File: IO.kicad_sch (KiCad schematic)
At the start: 7 parts

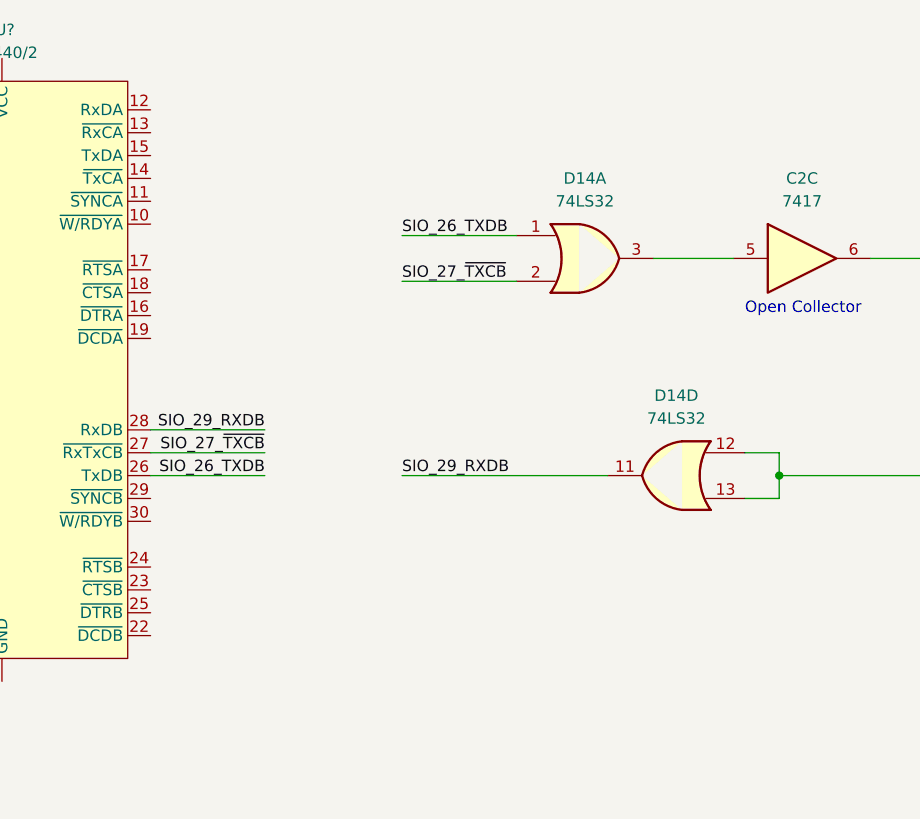
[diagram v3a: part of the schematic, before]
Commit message: Add SIOCLK jumper detail jumper details.
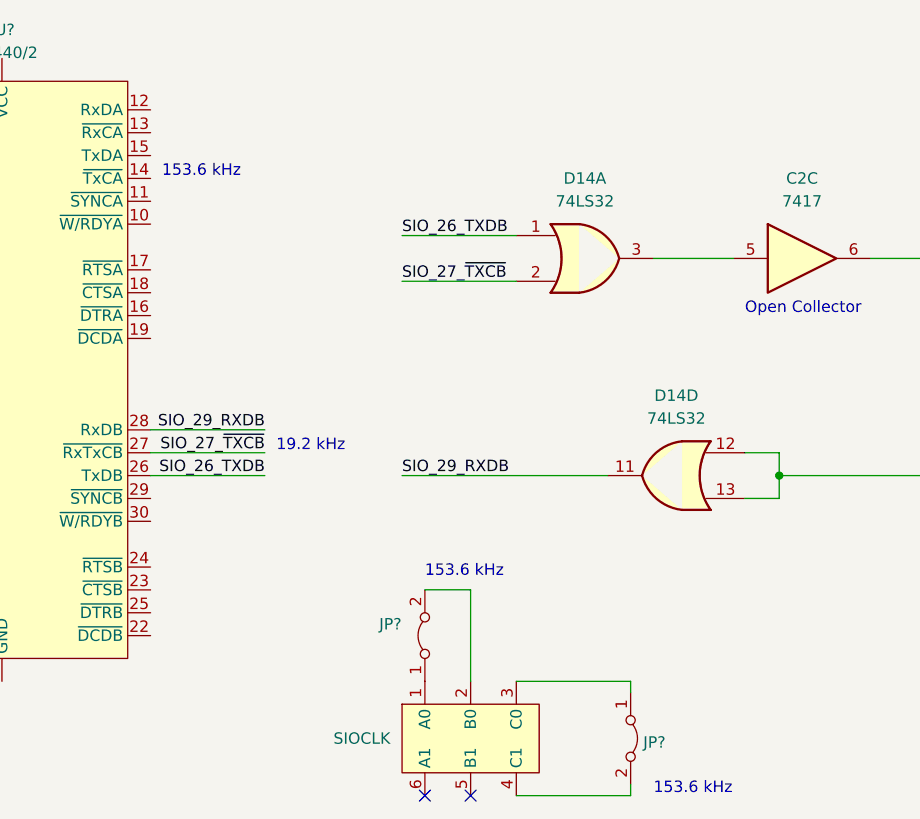
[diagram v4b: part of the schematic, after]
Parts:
- added J?: SIOCLK, symbol ceda:SIOCLK
- added JP? (x2): Jumper_2_Bridged, symbol Jumper:Jumper_2_Bridged
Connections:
- new net: J?.1 (A0), JP?.1 (A)
- new net: J?.2 (B0), JP?.2 (B)
- new net: J?.3 (C0), JP?.1 (A)
- new net: J?.4 (C1), JP?.2 (B)
- no-connect marks 0 -> 2
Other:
- note added: "153.6 kHz"
- note added: "19.2 kHz"
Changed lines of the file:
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@@
   (junction (at 167.64 54.61) (diameter 0) (color 0 0 0 0)
   )
+  (no_connect (at 78.74 114.3))
+  (no_connect (at 83.82 114.3))
   (wire (pts (xy 143.51 77.47) (xy 143.51 78.74))
     (stroke (width 0) (type default) (color 0 0 0 0))
@@
     (stroke (width 0) (type default) (color 0 0 0 0))
   )
+  (wire (pts (xy 88.9 114.3) (xy 101.6 114.3))
+    (stroke (width 0) (type default) (color 0 0 0 0))
+  )
   (wire (pts (xy 48.26 78.74) (xy 60.96 78.74))
     (stroke (width 0) (type default) (color 0 0 0 0))
@@
     (stroke (width 0) (type default) (color 0 0 0 0))
   )
+  (wire (pts (xy 101.6 114.3) (xy 101.6 113.03))
+    (stroke (width 0) (type default) (color 0 0 0 0))
+  )
   (wire (pts (xy 118.11 78.74) (xy 118.11 76.2))
     (stroke (width 0) (type default) (color 0 0 0 0))
@@
     (stroke (width 0) (type default) (color 0 0 0 0))
   )
+  (wire (pts (xy 101.6 101.6) (xy 101.6 102.87))
+    (stroke (width 0) (type default) (color 0 0 0 0))
+  )
   (wire (pts (xy 143.51 44.45) (xy 143.51 45.72))
     (stroke (width 0) (type default) (color 0 0 0 0))
@@
     (stroke (width 0) (type default) (color 0 0 0 0))
   )
+  (wire (pts (xy 78.74 91.44) (xy 83.82 91.44))
+    (stroke (width 0) (type default) (color 0 0 0 0))
+  )
   (wire (pts (xy 104.14 54.61) (xy 113.03 54.61))
     (stroke (width 0) (type default) (color 0 0 0 0))
   )
+  (wire (pts (xy 83.82 91.44) (xy 83.82 101.6))
+    (stroke (width 0) (type default) (color 0 0 0 0))
+  )
   (wire (pts (xy 167.64 62.23) (xy 167.64 54.61))
     (stroke (width 0) (type default) (color 0 0 0 0))
@@
     (stroke (width 0) (type default) (color 0 0 0 0))
   )
+  (wire (pts (xy 88.9 101.6) (xy 101.6 101.6))
+    (stroke (width 0) (type default) (color 0 0 0 0))
+  )
   (wire (pts (xy 76.2 52.07) (xy 88.9 52.07))
     (stroke (width 0) (type default) (color 0 0 0 0))
@@
   (wire (pts (xy 229.87 69.85) (xy 238.76 69.85))
     (stroke (width 0) (type default) (color 0 0 0 0))
+  )
+  (text "153.6 kHz" (at 104.14 114.3 0)
+    (effects (font (size 1.27 1.27)) (justify left bottom))
   )
   (text "Open Collector" (at 114.3 60.96 0)
@@
   (text "In realtà non ho idea di\nquale siano rx e tx, visto\nche sono cortocircuitati"
     (at 278.13 72.39 0)
+    (effects (font (size 1.27 1.27)) (justify left bottom))
+  )
+  (text "153.6 kHz" (at 49.53 45.72 0)
+    (effects (font (size 1.27 1.27)) (justify left bottom))
+  )
+  (text "153.6 kHz" (at 78.74 90.17 0)
+    (effects (font (size 1.27 1.27)) (justify left bottom))
+  )
+  (text "19.2 kHz" (at 62.23 76.2 0)
     (effects (font (size 1.27 1.27)) (justify left bottom))
   )
@@
     (pin "14")
     (pin "7")
+  )
+  (symbol (lib_id "ceda:SIOCLK") (at 83.82 107.95 0) (unit 1)
+    (in_bom yes) (on_board yes)
+    (property "Reference" "J?" (id 0) (at 72.39 105.41 0)
+      (effects (font (size 1.27 1.27)) (justify left) hide)
+    )
+    (property "Value" "SIOCLK" (id 1) (at 68.58 107.95 0)
+      (effects (font (size 1.27 1.27)) (justify left))
+    )
+    (property "Footprint" "" (id 2) (at 83.82 107.95 0)
+      (effects (font (size 1.27 1.27)) hide)
+    )
+    (property "Datasheet" "" (id 3) (at 83.82 107.95 0)
+      (effects (font (size 1.27 1.27)) hide)
+    )
+    (pin "1")
+    (pin "2")
+    (pin "3")
+    (pin "4")
+    (pin "5")
+    (pin "6")
   )
   (symbol (lib_id "power:+5V") (at 143.51 44.45 0) (unit 1)
@@
     (pin "8")
     (pin "9")
+  )
+  (symbol (lib_id "Jumper:Jumper_2_Bridged") (at 101.6 107.95 270) (unit 1)
+    (in_bom yes) (on_board yes) (fields_autoplaced)
+    (property "Reference" "JP?" (id 0) (at 102.997 108.3838 90)
+      (effects (font (size 1.27 1.27)) (justify left))
+    )
+    (property "Value" "Jumper_2_Bridged" (id 1) (at 102.997 109.6522 90)
+      (effects (font (size 1.27 1.27)) (justify left) hide)
+    )
+    (property "Footprint" "" (id 2) (at 101.6 107.95 0)
+      (effects (font (size 1.27 1.27)) hide)
+    )
+    (property "Datasheet" "~" (id 3) (at 101.6 107.95 0)
+      (effects (font (size 1.27 1.27)) hide)
+    )
+    (pin "1")
+    (pin "2")
   )
   (symbol (lib_id "power:+5V") (at 143.51 68.58 0) (unit 1)
@@
       (effects (font (size 1.27 1.27)) hide)
     )
+    (pin "1")
+    (pin "2")
+  )
+  (symbol (lib_id "Jumper:Jumper_2_Bridged") (at 78.74 96.52 90) (unit 1)
+    (in_bom yes) (on_board yes)
+    (property "Reference" "JP?" (id 0) (at 73.66 95.25 90)
+      (effects (font (size 1.27 1.27)) (justify right))
+    )
+    (property "Value" "Jumper_2_Bridged" (id 1) (at 59.69 97.79 90)
+      (effects (font (size 1.27 1.27)) (justify right) hide)
+    )
+    (property "Footprint" "" (id 2) (at 78.74 96.52 0)
+      (effects (font (size 1.27 1.27)) hide)
+    )
+    (property "Datasheet" "~" (id 3) (at 78.74 96.52 0)
+      (effects (font (size 1.27 1.27)) hide)
+    )

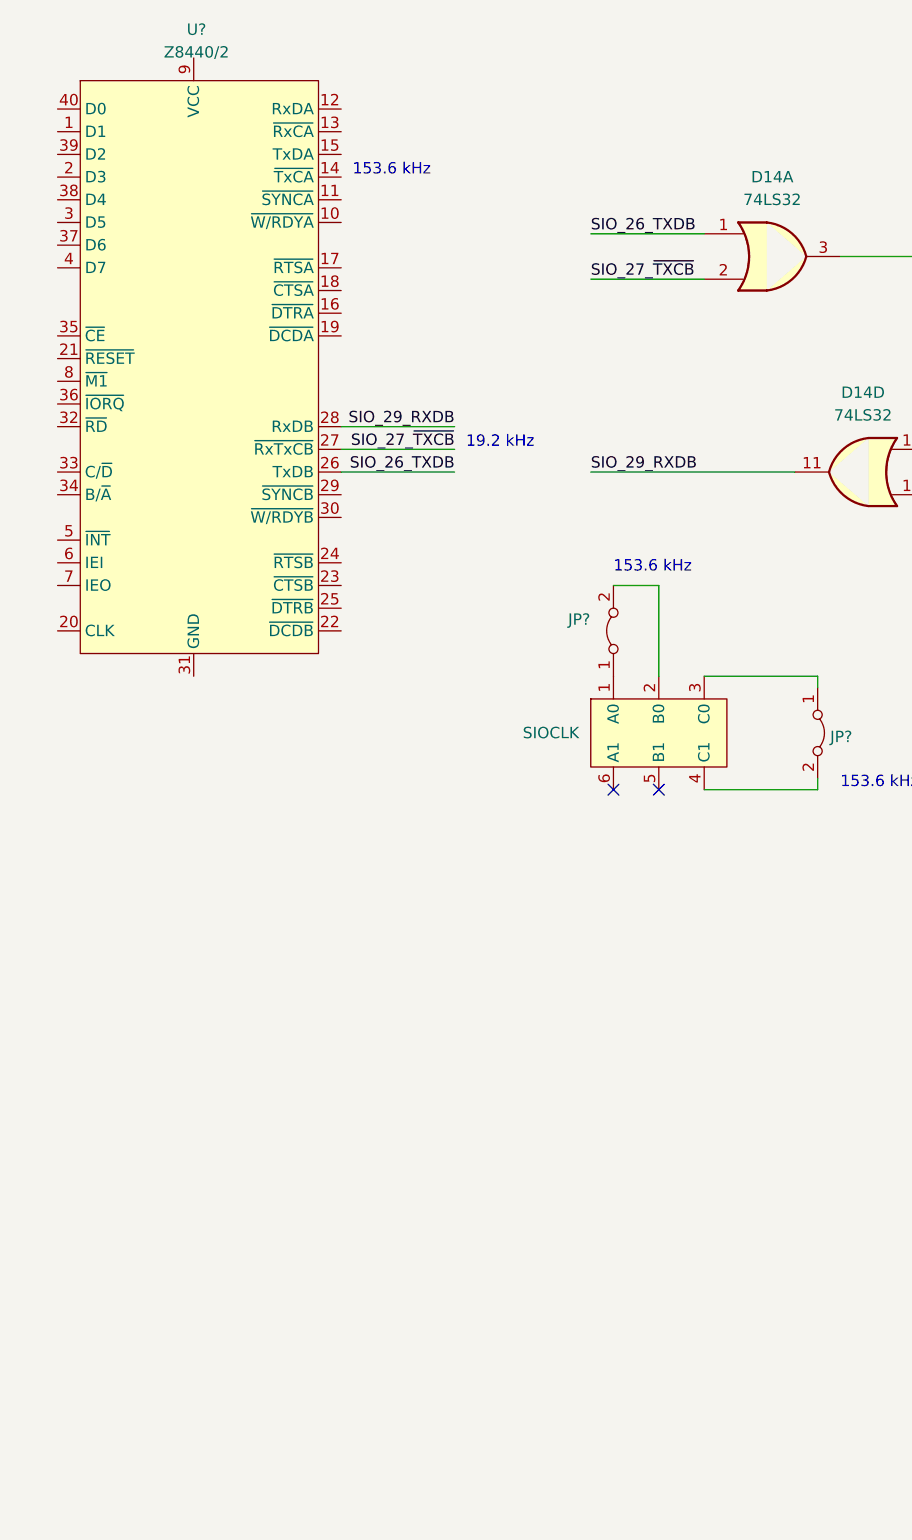
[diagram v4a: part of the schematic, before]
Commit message: Add address wires for SIO.
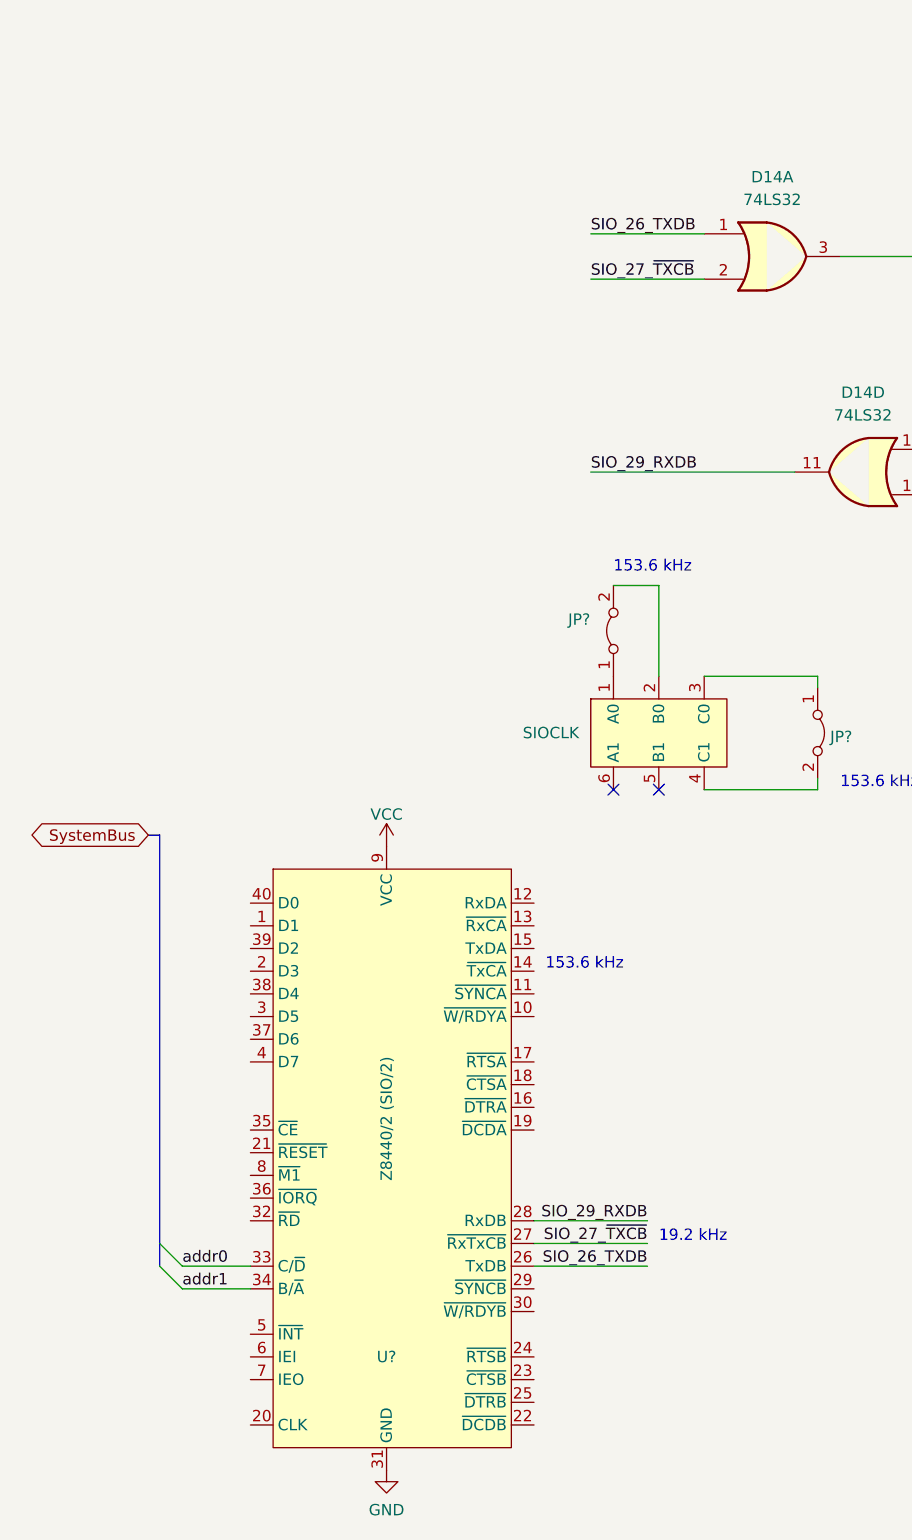
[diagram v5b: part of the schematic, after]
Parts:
- U?: value Z8440/2 -> Z8440/2 (SIO/2)
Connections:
- net GND: now reaches U?.31 (GND)
- net addr0: now reaches U?.33 (C/~{D})
- net addr1: now reaches U?.34 (B/~{A})
- net VCC: now reaches U?.9 (VCC)
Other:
- moved on the sheet: U?
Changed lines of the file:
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@@
   (no_connect (at 78.74 114.3))
   (no_connect (at 83.82 114.3))
+  (bus_entry (at 27.94 165.1) (size 2.54 2.54)
+    (stroke (width 0) (type default) (color 0 0 0 0))
+  )
+  (bus_entry (at 27.94 167.64) (size 2.54 2.54)
+    (stroke (width 0) (type default) (color 0 0 0 0))
+  )
   (wire (pts (xy 143.51 77.47) (xy 143.51 78.74))
     (stroke (width 0) (type default) (color 0 0 0 0))
@@
     (stroke (width 0) (type default) (color 0 0 0 0))
   )
-  (wire (pts (xy 48.26 78.74) (xy 60.96 78.74))
+  (wire (pts (xy 69.85 167.64) (xy 82.55 167.64))
     (stroke (width 0) (type default) (color 0 0 0 0))
   )
@@
     (stroke (width 0) (type default) (color 0 0 0 0))
   )
+  (wire (pts (xy 30.48 170.18) (xy 38.1 170.18))
+    (stroke (width 0) (type default) (color 0 0 0 0))
+  )
+  (wire (pts (xy 30.48 167.64) (xy 38.1 167.64))
+    (stroke (width 0) (type default) (color 0 0 0 0))
+  )
   (wire (pts (xy 232.41 41.91) (xy 238.76 41.91))
     (stroke (width 0) (type default) (color 0 0 0 0))
@@
     (stroke (width 0) (type default) (color 0 0 0 0))
   )
-  (wire (pts (xy 48.26 73.66) (xy 60.96 73.66))
+  (wire (pts (xy 69.85 162.56) (xy 82.55 162.56))
     (stroke (width 0) (type default) (color 0 0 0 0))
   )
@@
     (stroke (width 0) (type default) (color 0 0 0 0))
   )
+  (bus (pts (xy 26.67 119.38) (xy 27.94 119.38))
+    (stroke (width 0) (type default) (color 0 0 0 0))
+  )
   (wire (pts (xy 194.31 54.61) (xy 167.64 54.61))
     (stroke (width 0) (type default) (color 0 0 0 0))
@@
     (stroke (width 0) (type default) (color 0 0 0 0))
   )
+  (bus (pts (xy 27.94 167.64) (xy 27.94 165.1))
+    (stroke (width 0) (type default) (color 0 0 0 0))
+  )
   (wire (pts (xy 104.14 54.61) (xy 113.03 54.61))
     (stroke (width 0) (type default) (color 0 0 0 0))
@@
     (stroke (width 0) (type default) (color 0 0 0 0))
   )
+  (bus (pts (xy 27.94 165.1) (xy 27.94 119.38))
+    (stroke (width 0) (type default) (color 0 0 0 0))
+  )
   (wire (pts (xy 251.46 41.91) (xy 257.81 41.91))
     (stroke (width 0) (type default) (color 0 0 0 0))
@@
     (stroke (width 0) (type default) (color 0 0 0 0))
   )
-  (wire (pts (xy 48.26 76.2) (xy 60.96 76.2))
+  (wire (pts (xy 69.85 165.1) (xy 82.55 165.1))
     (stroke (width 0) (type default) (color 0 0 0 0))
   )
@@
     (effects (font (size 1.27 1.27)) (justify left bottom))
   )
-  (text "153.6 kHz" (at 49.53 45.72 0)
+  (text "153.6 kHz" (at 71.12 134.62 0)
     (effects (font (size 1.27 1.27)) (justify left bottom))
   )
@@
     (effects (font (size 1.27 1.27)) (justify left bottom))
   )
-  (text "19.2 kHz" (at 62.23 76.2 0)
+  (text "19.2 kHz" (at 83.82 165.1 0)
     (effects (font (size 1.27 1.27)) (justify left bottom))
   )
@@
     (effects (font (size 1.27 1.27)) (justify right bottom))
   )
-  (label "SIO_29_RXDB" (at 60.96 73.66 180)
-    (effects (font (size 1.27 1.27)) (justify right bottom))
+  (label "SIO_29_RXDB" (at 82.55 162.56 180)
+    (effects (font (size 1.27 1.27)) (justify right bottom))
+  )
+  (label "addr1" (at 30.48 170.18 0)
+    (effects (font (size 1.27 1.27)) (justify left bottom))
   )
   (label "SIO_26_TXDB" (at 76.2 52.07 0)
     (effects (font (size 1.27 1.27)) (justify left bottom))
   )
-  (label "SIO_26_TXDB" (at 60.96 78.74 180)
-    (effects (font (size 1.27 1.27)) (justify right bottom))
-  )
-  (label "SIO_27_~{TXCB}" (at 60.96 76.2 180)
+  (label "SIO_26_TXDB" (at 82.55 167.64 180)
+    (effects (font (size 1.27 1.27)) (justify right bottom))
+  )
+  (label "SIO_27_~{TXCB}" (at 82.55 165.1 180)
     (effects (font (size 1.27 1.27)) (justify right bottom))
   )
@@
     (effects (font (size 1.27 1.27)) (justify right bottom))
   )
+  (label "addr0" (at 30.48 167.64 0)
+    (effects (font (size 1.27 1.27)) (justify left bottom))
+  )
   (label "KBD_TX" (at 260.35 69.85 180)
     (effects (font (size 1.27 1.27)) (justify right bottom))
+  )
+  (global_label "SystemBus" (shape bidirectional) (at 26.67 119.38 180) (fields_autoplaced)
+    (effects (font (size 1.27 1.27)) (justify right))
+    (property "Riferimenti inter-foglio" "${INTERSHEET_REFS}" (id 0) (at 14.0969 119.3006 0)
+      (effects (font (size 1.27 1.27)) (justify right) hide)
+    )
   )
   (symbol (lib_id "74xx:74LS32") (at 106.68 78.74 0) (mirror y) (unit 4)
@@
     (pin "7")
   )
+  (symbol (lib_id "power:GND") (at 53.34 190.5 0) (unit 1)
+    (in_bom yes) (on_board yes) (fields_autoplaced)
+    (property "Reference" "#PWR?" (id 0) (at 53.34 196.85 0)
+      (effects (font (size 1.27 1.27)) hide)
+    )
+    (property "Value" "GND" (id 1) (at 53.34 194.9434 0))
+    (property "Footprint" "" (id 2) (at 53.34 190.5 0)
+      (effects (font (size 1.27 1.27)) hide)
+    )
+    (property "Datasheet" "" (id 3) (at 53.34 190.5 0)
+      (effects (font (size 1.27 1.27)) hide)
+    )
+    (pin "1")
+  )
   (symbol (lib_id "ceda:SIOCLK") (at 83.82 107.95 0) (unit 1)
     (in_bom yes) (on_board yes)
@@
     (pin "1")
   )
-  (symbol (lib_id "ceda:Z8440{slash}2") (at 31.75 63.5 0) (unit 1)
-    (in_bom yes) (on_board yes) (fields_autoplaced)
-    (property "Reference" "U?" (id 0) (at 32.0675 29.21 0))
-    (property "Value" "Z8440/2" (id 1) (at 32.0675 31.75 0))
-    (property "Footprint" "" (id 2) (at 26.035 48.895 0)
-      (effects (font (size 1.27 1.27)) hide)
-    )
-    (property "Datasheet" "" (id 3) (at 26.035 48.895 0)
-      (effects (font (size 1.27 1.27)) hide)
-    )
+  (symbol (lib_id "power:VCC") (at 53.34 120.65 0) (unit 1)
+    (in_bom yes) (on_board yes) (fields_autoplaced)
+    (property "Reference" "#PWR?" (id 0) (at 53.34 124.46 0)
+      (effects (font (size 1.27 1.27)) hide)
+    )
+    (property "Value" "VCC" (id 1) (at 53.34 117.0742 0))
+    (property "Footprint" "" (id 2) (at 53.34 120.65 0)
+      (effects (font (size 1.27 1.27)) hide)
+    )
+    (property "Datasheet" "" (id 3) (at 53.34 120.65 0)
+      (effects (font (size 1.27 1.27)) hide)
+    )
+    (pin "1")
+  )
+  (symbol (lib_id "ceda:Z8440{slash}2") (at 53.34 152.4 0) (unit 1)
+    (in_bom yes) (on_board yes) (fields_autoplaced)
+    (property "Reference" "U?" (id 0) (at 53.34 177.8 0))
+    (property "Value" "Z8440/2 (SIO/2)" (id 1) (at 53.34 151.13 90))
+    (property "Footprint" "" (id 2) (at 47.625 137.795 0)
+      (effects (font (size 1.27 1.27)) hide)
+    )
+    (property "Datasheet" "" (id 3) (at 47.625 137.795 0)
+      (effects (font (size 1.27 1.27)) hide)
+    )
